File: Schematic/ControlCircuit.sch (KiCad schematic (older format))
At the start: 27 parts, among them J1 JACK-PWR, Q1 TIP120, U1 LM555N, U2 ARDUINO_Pro-Mini, U3 74HC595, U4 74HC257, U5 74HC595, U6 MCP23S17

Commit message: V1.1.0 Realized that while the TLS5940 PWM Driver chip is using the SPI MOSI and SCK signals, the full signaling isn't SPI compatable. Specifically, the latch signal is high active where SPI CS is low active. Removed the SPI cleverness that allows many SPI devices with only 2 CS pins and daisy-chaned all 26 TLS5940s. Also changed the I/O Expander from SPI to I2C. Still need to decide on how to properly handle the unused PWM Driver outputs to keep the internal constant current channels from trying to pump current through and open circuit. Maybe add back-side LEDs for status signals? Also need to watch out for problems driving that many drivers. Might need to split up the groups between multiple µPs. Never the less, should be ready for prototype stage at this point.
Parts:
- removed C6, C7, C8: 0.1µF, symbol CAP_NP
- removed RN3, RN4: 10kΩ, symbol RN8BUSSIP
- removed U3, U5: 74HC595, symbol 74HC595
- removed U4: 74HC257, symbol 74HC257
- removed U6: MCP23S17, symbol MCP23S17
- added R305: 10kΩ, symbol RES
- added U303: MCP23017, symbol MCP23017
- R303: renamed from R3; CommonPartLibrary CPL-RES-THT-1.5K-0.25W -> CPL-POT-MULTI-25TURN-500-0.5W
- RN301: renamed from RN1; CommonPartLibrary CPL- -> CPL-RESARRAY-BUS7-THT-75-0.14W
- RN302: renamed from RN2; CommonPartLibrary CPL- -> CPL-RESARRAY-BUS7-THT-75-0.14W
- TP301: renamed from TP1; CommonPartLibrary (none) -> CPL-HDR-TESTPOINT; Mfg (none) -> Keystone; MfgPart (none) -> 5003
- renumbered C1 to C301, C2 to C302, C3 to C303, C4 to C304, C5 to C305, C9 to C306, J1 to J301, PS1 to PS301, Q1 to Q301, R1 to R301, R2 to R302, R4 to R304, U1 to U301, U2 to U302
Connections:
- net labels added: SCLK, SOUT, XLAT
- net labels removed: MISO, MOSI, MOSI', SCK, SCK', ~CS01, ~CS02, ~CS03, ~CS04, ~CS05, ~CS06, ~CS07, ~CS08, ~CS09, ~CS10, ~CS11, ~CS12, ~CS13, ~CS14, ~CS15, ~CS16, ~dCS, ~rCS
- wire segments 215 -> 111
- no-connect marks 20 -> 18
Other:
- moved on the sheet: C301, C302, C303, C304, C305, C306, J301, Q301, R301, R302, R303, R304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

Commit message: 1.1.1 Change TIP120 to TIP31C (on-hand stock), change Cap Ref'ds on LED Groups Fritzing file to plan perfboard layout for LED groups.
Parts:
- Q301: value TIP120 -> TIP31C; CommonPartLibrary CPL-TRN-NPN-60V-5A-THT -> CPL-TRN-NPN-100V-3A-THT; Mfg STMicroelectronics -> Fairchild Semiconductor; MfgPart TIP120 -> TIP31C
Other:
- moved on the sheet: U301B
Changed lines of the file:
@@
 Sheet 3 15
 Title "Interactive Rainbow"
-Date "2015-09-06"
-Rev "1.1.0"
+Date "2015-09-24"
+Rev "1.1.1"
 Comp "Sembazuru Circuit (for Barrel of Makers)"
 Comment1 "1.0.0 Initial Circuit"
 Comment2 "1.1.0 TLC5940 isn't actually SPI. Removed SPI cleverness and change I/O expander to I2C"
-Comment3 ""
+Comment3 "1.1.1 Change TIP120 to TIP31C (on-hand stock), change Cap Ref'ds on LED Groups"
 Comment4 ""
 $EndDescr
@@
 P 3950 2400
 F 0 "Q301" H 4200 2475 50  0000 L CNN
-F 1 "TIP120" H 4200 2400 50  0000 L CNN
+F 1 "TIP31C" H 4200 2400 50  0000 L CNN
 F 2 "TO-220" H 4200 2325 50  0001 L CIN
 F 3 "" H 3950 2400 50  0001 L CNN
-F 4 "CPL-TRN-NPN-60V-5A-THT" H 3950 2400 60  0001 C CNN "CommonPartLibrary"
-F 5 "STMicroelectronics" H 3950 2400 60  0001 C CNN "Mfg"
-F 6 "TIP120" H 3950 2400 60  0001 C CNN "MfgPart"
+F 4 "CPL-TRN-NPN-100V-3A-THT" H 3950 2400 60  0001 C CNN "CommonPartLibrary"
+F 5 "Fairchild Semiconductor" H 3950 2400 60  0001 C CNN "Mfg"
+F 6 "TIP31C" H 3950 2400 60  0001 C CNN "MfgPart"
 	1    3950 2400
 	1    0    0    -1
@@
 L LM555N U301
 U 2 1 55EAB65C
-P 2600 7000
-F 0 "U301" H 2400 7300 60  0000 C CNN
-F 1 "LM555N" H 2600 7000 60  0000 C CNB
-F 2 "" H 2600 7000 60  0000 C CNN
-F 3 "" H 2600 7000 60  0000 C CNN
-F 4 "CPL-LIC-TIMER-555" H 2600 7000 60  0001 C CNN "CommonPartLibrary"
-F 5 "Texas Instruments" H 2600 7000 60  0001 C CNN "Mfg"
-F 6 "NE555P" H 2600 7000 60  0001 C CNN "MfgPart"
-	2    2600 7000
+P 1400 7000
+F 0 "U301" H 1200 7300 60  0000 C CNN
+F 1 "LM555N" H 1400 7000 60  0000 C CNB
+F 2 "" H 1400 7000 60  0000 C CNN
+F 3 "" H 1400 7000 60  0000 C CNN
+F 4 "CPL-LIC-TIMER-555" H 1400 7000 60  0001 C CNN "CommonPartLibrary"
+F 5 "Texas Instruments" H 1400 7000 60  0001 C CNN "Mfg"
+F 6 "NE555P" H 1400 7000 60  0001 C CNN "MfgPart"
+	2    1400 7000
 	1    0    0    -1
 $EndComp
@@
 L MCP23017 U303
 U 2 1 55ECA5E7
-P 1400 7000
-F 0 "U303" H 1100 7300 60  0000 L CNN
-F 1 "MCP23017" H 1400 7000 60  0000 C CNB
-F 2 "" H 1400 7000 60  0000 C CNN
-F 3 "" H 1400 7000 60  0000 C CNN
-F 4 "CPL-" H 1400 7000 60  0001 C CNN "CommonPartLibrary"
-	2    1400 7000
-	1    0    0    -1
-$EndComp
+P 2600 7000
+F 0 "U303" H 2300 7300 60  0000 L CNN
+F 1 "MCP23017" H 2600 7000 60  0000 C CNB
+F 2 "" H 2600 7000 60  0000 C CNN
+F 3 "" H 2600 7000 60  0000 C CNN
+F 4 "CPL-" H 2600 7000 60  0001 C CNN "CommonPartLibrary"
+	2    2600 7000
+	1    0    0    -1
+$EndComp

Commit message: Updated schematic for simplified auto-cycling leds. Lower part count and cost, not as flexible on color cycling.
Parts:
- removed C306: 0.1µF, symbol CAP_NP
- removed PS301: Pololu_S10V4F5, symbol Pololu_S10V4F5
- removed R305: 10kΩ, symbol RES
- removed U303: MCP23017, symbol MCP23017
- added C207, C208, C209, C210: 0.1µF, symbol CAP_NP
- added PS201: Pololu_S18V20F5, symbol Pololu_S18V20F5
- added Q202: 2N2222, symbol Q_NPN_EBC
- added R205, R206: 1.0kΩ, symbol RES
- added U203, U204: 74HC595, symbol 74HC595
- added U205, U206: 74HC165, symbol 74HC165
- C201: renamed from C301; MfgPart C315C103K1R5TA -> C215C103K1R5TA
- C202: renamed from C302; MfgPart C315C103K1R5TA -> C215C103K1R5TA
- C204: renamed from C304; MfgPart C320C104K5R5TA -> C220C104K5R5TA
- C205: renamed from C305; MfgPart C320C104K5R5TA -> C220C104K5R5TA
- J201: renamed from J301; CommonPartLibrary CPL- -> CPL-CON-BARREL-THT-2.1MM
- renumbered C303 to C203, Q301 to Q201, R301 to R201, R302 to R202, R303 to R203, R304 to R204, RN301 to RN201, RN302 to RN202, TP301 to TP201, U301 to U201, U302 to U202
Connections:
- net labels added: All_Blue/White, All_Brown/White, All_Green, All_Green/White, All_Orange, Blue01, Blue02, Blue03, Blue04, Blue05, Blue06, Blue07, Blue08, Blue09, Blue10, Blue11, Blue12, Blue13, Brown01, Brown02, Brown03, Brown04, Brown05, Brown06, Brown07, Brown08, Brown09, Brown10, Brown11, Brown12, Brown13, IR_5V, IR_GND, LED01, LED02, LED03, LED04, LED05, LED06, LED07, LED08, LED09, LED10, LED11, LED12, LED13, LED_5V, LED_GND1, LED_GND2, Orange/White01, Orange/White02, Orange/White03, Orange/White04, Orange/White05, Orange/White06, Orange/White07, Orange/White08, Orange/White09, Orange/White10, Orange/White11, Orange/White12, Orange/White13
- net labels removed: BLANK, GSCLK, SCLK, SOUT, XLAT
- wire segments 111 -> 169
- no-connect marks 18 -> 30
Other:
- moved on the sheet: C201, C202, C203, C204, C205, J201, Q201, R201, R202, R203, R204, RN201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

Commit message: Change TIP31C to 2N2222. (Don't need the current capacity, so why pay for it?) Clean-up BOM items.
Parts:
- removed Q201: TIP31C, TO-220, symbol TIP120
- added Q201: 2N2222, symbol Q_NPN_EBC
- C201, C202: MfgPart C215C103K1R5TA -> C315C103K1R5TA
- C203: CommonPartLibrary CPL-CAP-TANT-THT-10UF-25V -> CPL-CAP-TANT-THT-10UF-50V*; MfgPart TAP106K025CRW -> TAP106K050SCS
- C204, C205, C207, C208, C209, C210: MfgPart C220C104K5R5TA -> C320C104K5R5TA
- J201: CommonPartLibrary CPL-CON-BARREL-THT-2.1MM -> CPL-CON-BARREL-THT-2.1MM*
- PS201: CommonPartLibrary CPL-REG-SWI-5V-2A-BREAKOUT -> CPL-REG-SWI-5V-2A-BREAKOUT*
- R201: CommonPartLibrary CPL-RES-THT-75.0-0.25W -> CPL-RES-THT-75-0.25W*
- R203: value 500Ω -> 1kΩ; CommonPartLibrary CPL-POT-MULTI-25TURN-500-0.5W -> CPL-POT-MULTI-25TURN-1K-0.5W; MfgPart 3296W-1-501LF -> 3296W-1-102LF
- R204: value 1.5kΩ -> 1.3kΩ; CommonPartLibrary CPL-RES-THT-1.5K-0.25W -> CPL-RES-THT-1.3K-0.25W*; MfgPart MFR-25FBF52-1K5 -> MFR-25FBF52-1K3
- R205, R206: value 1.0kΩ -> 1kΩ
- RN201, RN202: CommonPartLibrary CPL-RESARRAY-BUS7-THT-75-0.14W -> CPL-ARR-BUS7-THT-75-0.14W*
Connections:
- net GND: now also Q201.1 (E)
- net at R202.2: now also Q201.2 (B)
- net at RN201.1 (C), RN202.1 (C): now also Q201.3 (C)
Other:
- note added: "Trim for\n38kHz\nat pin3\n(ideally\nR203+R204\n=1.8kΩ)"
- note removed: "Trim for\n38kHz\nat pin3"
- moved on the sheet: C203, C204, J201, PS201

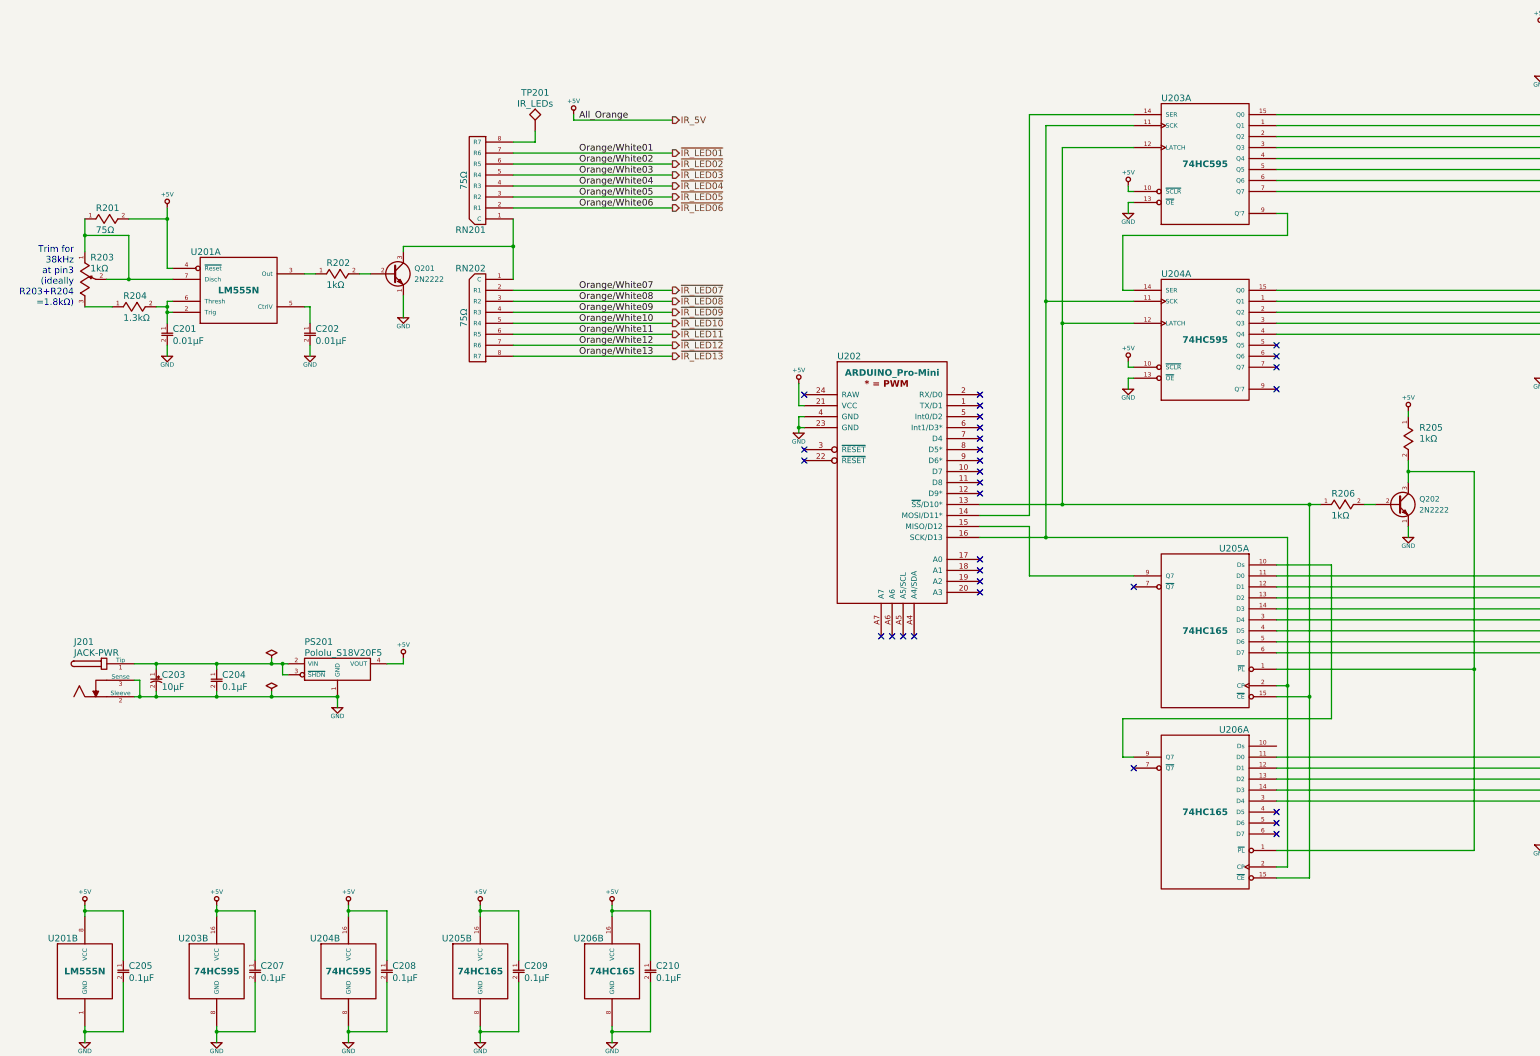
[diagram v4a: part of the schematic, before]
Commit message: v1.2.2 Change 555 to CMOS 7555 to simplify IR strobe design & lower current. And, control IR LEDs to only light when SPI transfer.
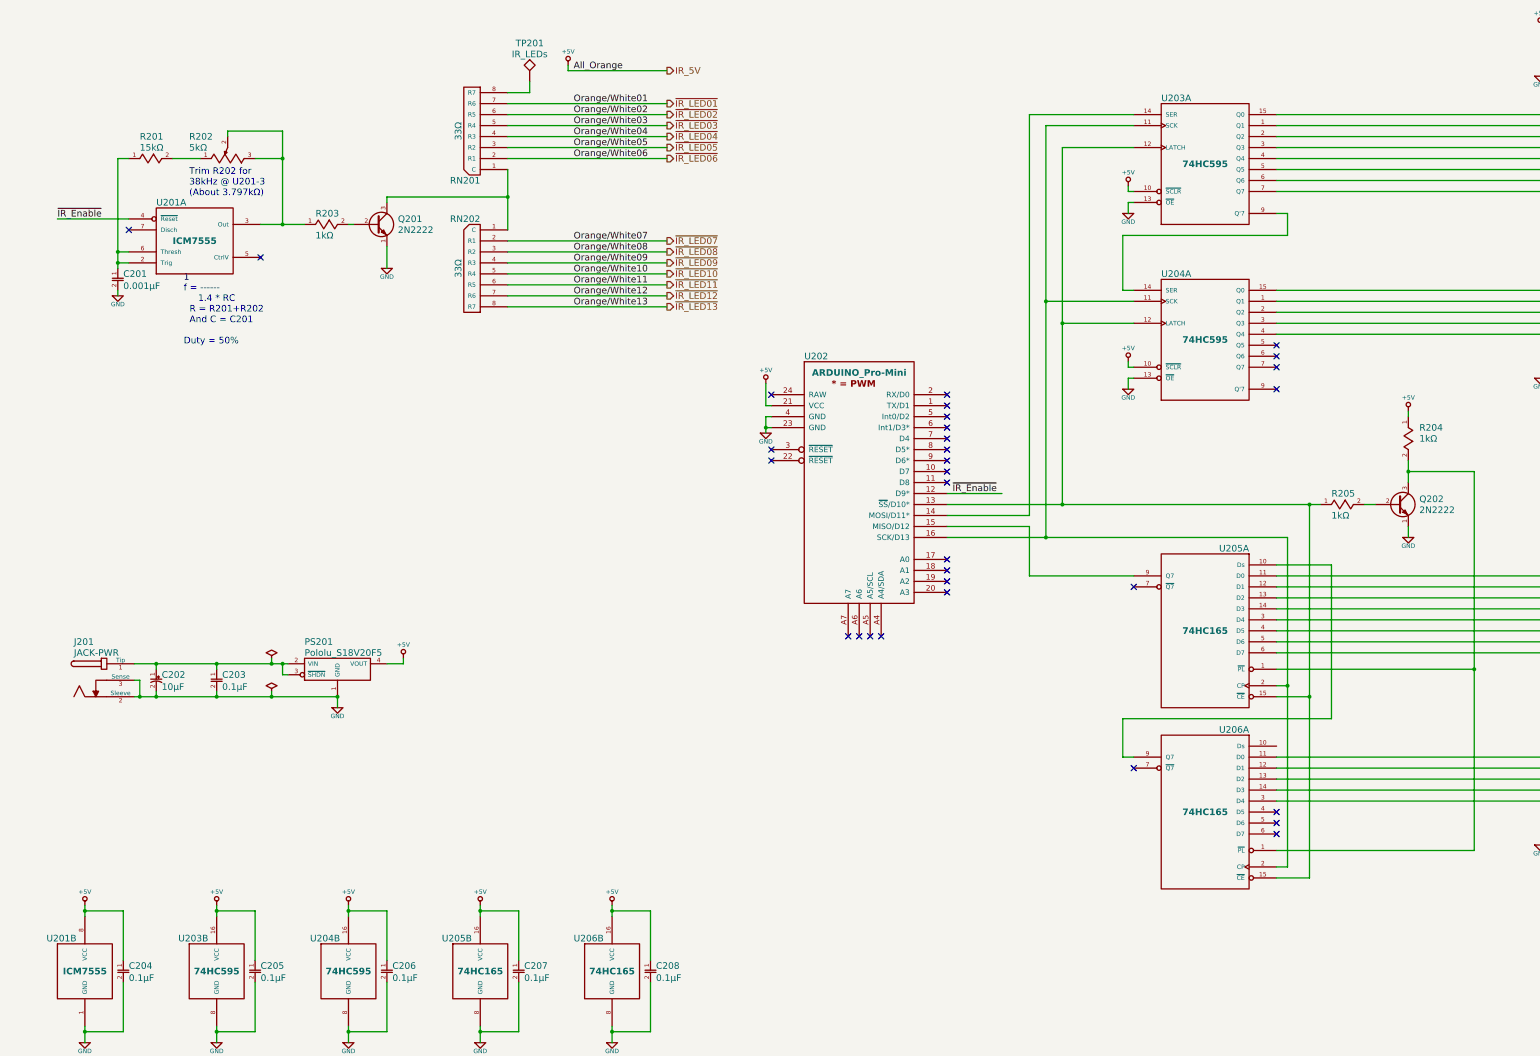
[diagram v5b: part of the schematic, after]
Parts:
- removed C202: 0.01µF, symbol CAP_NP
- removed R204: 1.3kΩ, symbol RES
- removed U201: LM555N, symbol LM555N
- added U201: ICM7555, symbol ICM7555
- C201: value 0.01µF -> 0.001µF; CommonPartLibrary CPL-CAP-X7R-THT-10NF-100V -> CPL-CAP-X7R-THT-1NF-100V; MfgPart C315C103K1R5TA -> C315C102K1R5TA
- R201: value 75Ω -> 15kΩ; CommonPartLibrary CPL-RES-THT-75-0.25W* -> CPL-RES-THT-15K-0.25W*; MfgPart MFR-25FBF52-75R -> MFR-25FBF52-15K
- R202: renamed from R203; value 1kΩ -> 5kΩ; CommonPartLibrary CPL-POT-MULTI-25TURN-1K-0.5W -> CPL-POT-MULTI-25TURN-5K-0.5W*; MfgPart 3296W-1-102LF -> 3296W-1-502LF
- RN201, RN202: value 75Ω -> 33Ω; CommonPartLibrary CPL-ARR-BUS7-THT-75-0.14W* -> CPL-ARR-BUS7-THT-33-0.14W*; MfgPart 4308R-101-750LF -> 4308R-101-330
- renumbered C203 to C202, C204 to C203, C210 to C204, C209 to C206, R202 to R203, R205 to R204, R206 to R205
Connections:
- net +5V: now also U201.8 (VCC); no longer R201.2
- net GND: now also U201.1 (GND)
- net ~IR_Enable: now reaches U202.12 (D9*)
- net ~IR_Enable: now also U201.4 (~Reset)
- net at C201.1: now also R201.1, U201.2 (Trig), U201.6 (Thresh)
- net at R203.1: now also R202.2 (Wiper), R202.3, U201.3 (Out)
- new net: R201.2, R202.1
- no-connect marks 30 -> 31
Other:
- note added: "1\nf = ------\n 1.4 * RC\n R = R201+R202\n And C = C201\n\nDuty = 50%"
- note added: "Trim R202 for\n38kHz @ U201-3\n(About 3.797kΩ)"
- note removed: "Trim for\n38kHz\nat pin3\n(ideally\nR203+R204\n=1.8kΩ)"
- moved on the sheet: C201, C204, C205, C206, C207, C208, Q201, R201, R202, R203, RN201, RN202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

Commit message: v1.2.3 Correct 7555 enable logic level to high active. (Also remembered to put latest schematic pdf in repository)
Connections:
- net ~IR_Enable renamed IR_Enable
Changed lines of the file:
@@
 Sheet 2 15
 Title "Interactive Rainbow"
-Date "2015-12-16"
-Rev "1.2.2"
+Date "2016-01-09"
+Rev "1.2.3"
 Comp "Sembazuru Circuit (for Barrel of Makers)"
-Comment1 "1.1.1 Change TIP120 to TIP31C (on-hand stock), change Cap Ref'ds on LED Groups"
-Comment2 "1.2.0 Change design to use LEDs with integrated flashing. Simpler design."
-Comment3 "1.2.1 Chance TIP31C to 2N2222. Don't need extra current capacity."
-Comment4 "1.2.2 Change 555 to CMOS 7555 to simplify IR strobe design & lower current."
+Comment1 "1.2.0 Change design to use LEDs with integrated flashing. Simpler design."
+Comment2 "1.2.1 Chance TIP31C to 2N2222. Don't need extra current capacity."
+Comment3 "1.2.2 Change 555 to CMOS 7555 to simplify IR strobe design & lower current."
+Comment4 "1.2.3 Correct 7555 enable logic level to high active."
 $EndDescr
 $Comp
@@
 NoConn ~ 2800 2900
 Text Label 950  2550 0    60   ~ 0
-~IR_Enable
+IR_Enable
 Text Label 9100 5050 0    60   ~ 0
-~IR_Enable
+IR_Enable
 Wire Wire Line
 	1600 2550 950  2550
